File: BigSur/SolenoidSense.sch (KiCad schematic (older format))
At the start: 34 parts, among them U10 MCP6L02T-E_MS, U11 74LVC1G00W5-7, U12 ACS70331EESATR-2P5U3, U5 ACS70331EESATR-2P5U3, U6 ACS70331EESATR-2P5U3, U7 ACS70331EESATR-2P5U3, U8 ACS70331EESATR-2P5U3, U9 ACS70331EESATR-2P5U3

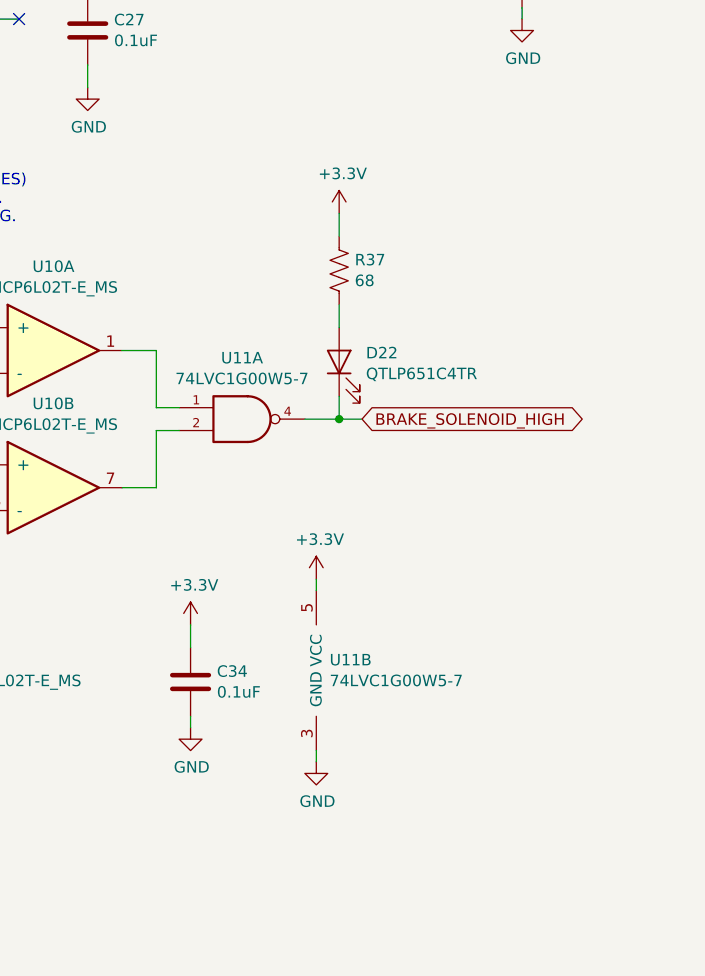
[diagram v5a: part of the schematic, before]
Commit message: Fixed braking LED direction
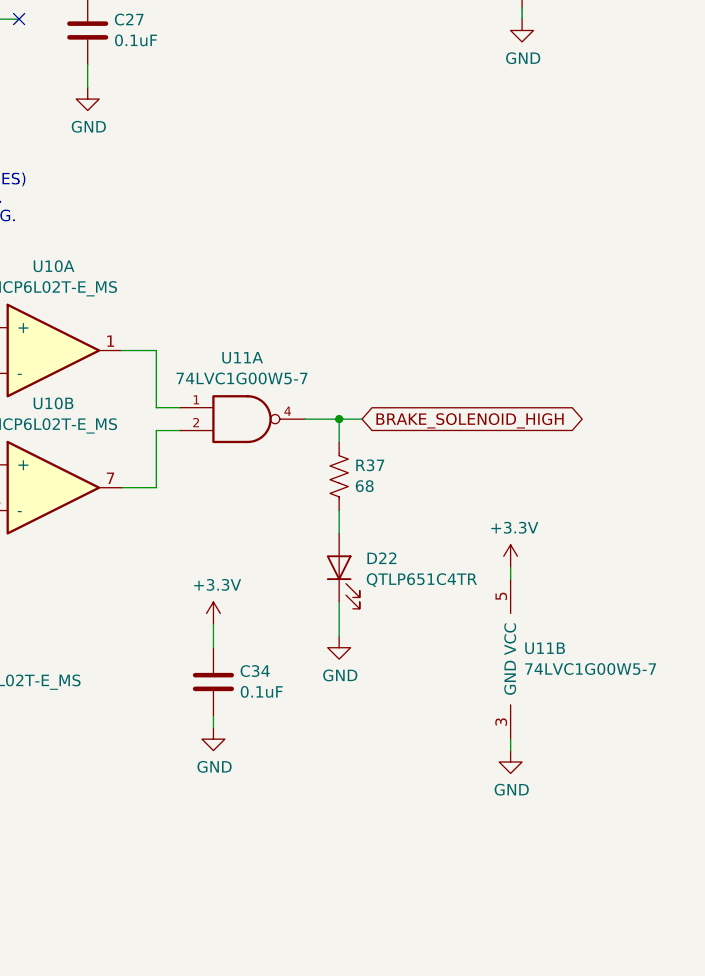
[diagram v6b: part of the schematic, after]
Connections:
- net +3V3: no longer R37.1
- net BRAKE_SOLENOID_HIGH: now also R37.1; no longer D22.1 (K)
- net GND: now also D22.1 (K)
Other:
- moved on the sheet: C34, D22, R37, U11B
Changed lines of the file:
@@
 EESchema Schematic File Version 4
 LIBS:BigSur-cache
-EELAYER 29 0
+EELAYER 30 0
 EELAYER END
 $Descr A4 11693 8268
@@
 L power:+3.3V #PWR0110
 U 1 1 5DAF6490
-P 9650 5450
-F 0 "#PWR0110" H 9650 5300 50  0001 C CNN
-F 1 "+3.3V" H 9665 5623 50  0000 C CNN
-F 2 "" H 9650 5450 50  0001 C CNN
-F 3 "" H 9650 5450 50  0001 C CNN
-	1    9650 5450
-	1    0    0    -1
-$EndComp
-Wire Wire Line
-	9650 5450 9650 5500
-Wire Wire Line
-	9650 6200 9650 6250
+P 10500 5400
+F 0 "#PWR0110" H 10500 5250 50  0001 C CNN
+F 1 "+3.3V" H 10515 5573 50  0000 C CNN
+F 2 "" H 10500 5400 50  0001 C CNN
+F 3 "" H 10500 5400 50  0001 C CNN
+	1    10500 5400
+	1    0    0    -1
+$EndComp
+Wire Wire Line
+	10500 5400 10500 5450
+Wire Wire Line
+	10500 6150 10500 6200
 $Comp
 L power:GND #PWR0120
 U 1 1 5DAF8FA9
-P 9650 6250
-F 0 "#PWR0120" H 9650 6000 50  0001 C CNN
-F 1 "GND" H 9655 6077 50  0000 C CNN
-F 2 "" H 9650 6250 50  0001 C CNN
-F 3 "" H 9650 6250 50  0001 C CNN
-	1    9650 6250
+P 10500 6200
+F 0 "#PWR0120" H 10500 5950 50  0001 C CNN
+F 1 "GND" H 10505 6027 50  0000 C CNN
+F 2 "" H 10500 6200 50  0001 C CNN
+F 3 "" H 10500 6200 50  0001 C CNN
+	1    10500 6200
 	1    0    0    -1
 $EndComp
@@
 L power:GND #PWR0118
 U 1 1 5DB0D1A1
-P 9100 6100
-F 0 "#PWR0118" H 9100 5850 50  0001 C CNN
-F 1 "GND" H 9105 5927 50  0000 C CNN
-F 2 "" H 9100 6100 50  0001 C CNN
-F 3 "" H 9100 6100 50  0001 C CNN
-	1    9100 6100
-	1    0    0    -1
-$EndComp
-Wire Wire Line
-	9100 6050 9100 6100
+P 9200 6100
+F 0 "#PWR0118" H 9200 5850 50  0001 C CNN
+F 1 "GND" H 9205 5927 50  0000 C CNN
+F 2 "" H 9200 6100 50  0001 C CNN
+F 3 "" H 9200 6100 50  0001 C CNN
+	1    9200 6100
+	1    0    0    -1
+$EndComp
+Wire Wire Line
+	9200 6050 9200 6100
 $Comp
 L Device:C C?
 U 1 1 5DB0D1AF
-P 9100 5900
+P 9200 5900
 AR Path="/5D6EB2B2/5DB0D1AF" Ref="C?"  Part="1"
 AR Path="/5D71C3EA/5DB0D1AF" Ref="C?"  Part="1"
 AR Path="/5D765C4F/5DB0D1AF" Ref="C34"  Part="1"
-F 0 "C34" H 9215 5946 50  0000 L CNN
-F 1 "0.1uF" H 9215 5855 50  0000 L CNN
-F 2 "Capacitor_SMD:C_0603_1608Metric_Pad1.05x0.95mm_HandSolder" H 9100 5900 50  0001 C CNN
-F 3 "http://www.samsungsem.com/kr/support/product-search/mlcc/__icsFiles/afieldfile/2019/06/18/CL10B104KB8NNNC-19.pdf" H 9100 5900 50  0001 C CNN
-F 4 "CL10B104KB8NNNC" H 9100 5900 50  0001 C CNN "Part Number"
-F 5 "https://www.digikey.ca/product-detail/en/samsung-electro-mechanics/CL10B104KB8NNNC/1276-1000-1-ND/3889086" H 9100 5900 50  0001 C CNN "Digikey"
-	1    9100 5900
+F 0 "C34" H 9315 5946 50  0000 L CNN
+F 1 "0.1uF" H 9315 5855 50  0000 L CNN
+F 2 "Capacitor_SMD:C_0603_1608Metric_Pad1.05x0.95mm_HandSolder" H 9200 5900 50  0001 C CNN
+F 3 "http://www.samsungsem.com/kr/support/product-search/mlcc/__icsFiles/afieldfile/2019/06/18/CL10B104KB8NNNC-19.pdf" H 9200 5900 50  0001 C CNN
+F 4 "CL10B104KB8NNNC" H 9200 5900 50  0001 C CNN "Part Number"
+F 5 "https://www.digikey.ca/product-detail/en/samsung-electro-mechanics/CL10B104KB8NNNC/1276-1000-1-ND/3889086" H 9200 5900 50  0001 C CNN "Digikey"
+	1    9200 5900
 	1    0    0    -1
 $EndComp
@@
 L power:+3.3V #PWR0114
 U 1 1 5DB161C4
-P 9100 5650
-F 0 "#PWR0114" H 9100 5500 50  0001 C CNN
-F 1 "+3.3V" H 9115 5823 50  0000 C CNN
-F 2 "" H 9100 5650 50  0001 C CNN
-F 3 "" H 9100 5650 50  0001 C CNN
-	1    9100 5650
-	1    0    0    -1
-$EndComp
-Wire Wire Line
-	9100 5650 9100 5750
+P 9200 5650
+F 0 "#PWR0114" H 9200 5500 50  0001 C CNN
+F 1 "+3.3V" H 9215 5823 50  0000 C CNN
+F 2 "" H 9200 5650 50  0001 C CNN
+F 3 "" H 9200 5650 50  0001 C CNN
+	1    9200 5650
+	1    0    0    -1
+$EndComp
+Wire Wire Line
+	9200 5650 9200 5750
 Text GLabel 9850 4750 2    50   BiDi ~ 0
 BRAKE_SOLENOID_HIGH
@@
 L Device:LED D22
 U 1 1 5DC1B64C
-P 9750 4500
-F 0 "D22" V 9789 4383 50  0000 R CNN
-F 1 "QTLP651C4TR" V 9698 4383 50  0000 R CNN
-F 2 "LED_SMD:LED_1206_3216Metric_Pad1.42x1.75mm_HandSolder" H 9750 4500 50  0001 C CNN
-F 3 "https://media.digikey.com/pdf/Data%20Sheets/Everlight%20PDFs/QTLP651C-2,3,4,7,B.pdf" H 9750 4500 50  0001 C CNN
-F 4 "https://www.digikey.ca/product-detail/en/everlight-electronics-co-ltd/QTLP651C4TR/1080-1484-1-ND/7598723" V 9750 4500 50  0001 C CNN "Digikey"
-	1    9750 4500
+P 9750 5400
+F 0 "D22" V 9789 5283 50  0000 R CNN
+F 1 "QTLP651C4TR" V 9698 5283 50  0000 R CNN
+F 2 "LED_SMD:LED_1206_3216Metric_Pad1.42x1.75mm_HandSolder" H 9750 5400 50  0001 C CNN
+F 3 "https://media.digikey.com/pdf/Data%20Sheets/Everlight%20PDFs/QTLP651C-2,3,4,7,B.pdf" H 9750 5400 50  0001 C CNN
+F 4 "https://www.digikey.ca/product-detail/en/everlight-electronics-co-ltd/QTLP651C4TR/1080-1484-1-ND/7598723" V 9750 5400 50  0001 C CNN "Digikey"
+	1    9750 5400
 	0    -1   -1   0
 $EndComp
-Wire Wire Line
-	9750 4650 9750 4750
 Connection ~ 9750 4750
 Wire Wire Line
@@
 L Device:R_US R37
 U 1 1 5DC2971E
-P 9750 4100
-F 0 "R37" H 9818 4146 50  0000 L CNN
-F 1 "68" H 9818 4055 50  0000 L CNN
-F 2 "Resistor_SMD:R_0603_1608Metric_Pad1.05x0.95mm_HandSolder" V 9790 4090 50  0001 C CNN
-F 3 "https://www.rohm.com/datasheet/ESR01MZPF/esr-e" H 9750 4100 50  0001 C CNN
-F 4 "https://www.digikey.ca/product-detail/en/rohm-semiconductor/ESR03EZPJ680/RHM68DCT-ND/4053812" H 9750 4100 50  0001 C CNN "Digikey"
-F 5 "ESR03EZPJ680" H 9750 4100 50  0001 C CNN "Part Number"
-	1    9750 4100
-	1    0    0    -1
-$EndComp
-Wire Wire Line
-	9750 4250 9750 4350
-$Comp
-L power:+3.3V #PWR0101
-U 1 1 5DC3736E
-P 9750 3850
-F 0 "#PWR0101" H 9750 3700 50  0001 C CNN
-F 1 "+3.3V" H 9765 4023 50  0000 C CNN
-F 2 "" H 9750 3850 50  0001 C CNN
-F 3 "" H 9750 3850 50  0001 C CNN
-	1    9750 3850
-	1    0    0    -1
-$EndComp
-Wire Wire Line
-	9750 3850 9750 3950
+P 9750 5000
+F 0 "R37" H 9818 5046 50  0000 L CNN
+F 1 "68" H 9818 4955 50  0000 L CNN
+F 2 "Resistor_SMD:R_0603_1608Metric_Pad1.05x0.95mm_HandSolder" V 9790 4990 50  0001 C CNN
+F 3 "https://www.rohm.com/datasheet/ESR01MZPF/esr-e" H 9750 5000 50  0001 C CNN
+F 4 "https://www.digikey.ca/product-detail/en/rohm-semiconductor/ESR03EZPJ680/RHM68DCT-ND/4053812" H 9750 5000 50  0001 C CNN "Digikey"
+F 5 "ESR03EZPJ680" H 9750 5000 50  0001 C CNN "Part Number"
+	1    9750 5000
+	1    0    0    -1
+$EndComp
+Wire Wire Line
+	9750 5150 9750 5250
+Wire Wire Line
+	9750 4750 9750 4850
 Wire Wire Line
 	6100 4700 6450 4700
@@
 L BigSurLib:74LVC1G00W5-7 U11
 U 2 1 5DD4ED6F
-P 9650 5850
-F 0 "U11" H 9708 5896 50  0000 L CNN
-F 1 "74LVC1G00W5-7" H 9708 5805 50  0000 L CNN
-F 2 "Package_TO_SOT_SMD:SOT-23-5" H 9700 6050 50  0001 C CNN
-F 3 "https://www.diodes.com/assets/Datasheets/74LVC1G08.pdf" H 9700 5850 50  0001 C CNN
-F 4 "https://www.digikey.ca/product-detail/en/diodes-incorporated/74LVC1G00W5-7/1034-74LVC1G00W5-7DICT-ND/5629187" H 9900 6150 50  0001 C CNN "Digikey"
-	2    9650 5850
+P 10500 5800
+F 0 "U11" H 10558 5846 50  0000 L CNN
+F 1 "74LVC1G00W5-7" H 10558 5755 50  0000 L CNN
+F 2 "Package_TO_SOT_SMD:SOT-23-5" H 10550 6000 50  0001 C CNN
+F 3 "https://www.diodes.com/assets/Datasheets/74LVC1G08.pdf" H 10550 5800 50  0001 C CNN
+F 4 "https://www.digikey.ca/product-detail/en/diodes-incorporated/74LVC1G00W5-7/1034-74LVC1G00W5-7DICT-ND/5629187" H 10750 6100 50  0001 C CNN "Digikey"
+	2    10500 5800
 	1    0    0    -1
 $EndComp
@@
 	1    0    0    -1
 $EndComp
+Wire Wire Line
+	9750 5550 9750 5700
+$Comp
+L power:GND #PWR?
+U 1 1 5DDEDFE6
+P 9750 5700
+F 0 "#PWR?" H 9750 5450 50  0001 C CNN
+F 1 "GND" H 9755 5527 50  0000 C CNN
+F 2 "" H 9750 5700 50  0001 C CNN
+F 3 "" H 9750 5700 50  0001 C CNN
+	1    9750 5700
+	1    0    0    -1
+$EndComp
